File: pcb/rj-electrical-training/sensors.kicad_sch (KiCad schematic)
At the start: 13 parts, among them IC1 IS31FL3254-QFLS4-TR, IC2 LM75ADP,118, U10 TMAG5273C1QDBVR, U7 ICM-42605, U8 VEML3328, U9 TCA9534PWR

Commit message: Updated sensor schematics and GPIO expander
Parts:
- added C27: 0.1u, TMAG5273C1QDBVR:SOT95P280X140-6N, symbol Device:C
- added C28: 1u, TMAG5273C1QDBVR:SOT95P280X140-6N, symbol Device:C
- added C29: 100nF, TMAG5273C1QDBVR:SOT95P280X140-6N, symbol Device:C
- added LED1, LED2, LED4, LED5, LED6, LED7, LED8, LED9: CLMVC-FKA-CL1D1L71BB7C3C3, CLMVC-FKA-CL1D1L71BB7C3C3_CRE, symbol 2026-10-25_23-53-28:CLMVC-FKA-CL1D1L71BB7C3C3
- added RN1: YC158TJR-0710KL, YC158TJR-0710KL:RESCAXE64P320X160X70-10N, symbol YC158TJR-0710KL:YC158TJR-0710KL
- added S1: DS01C-254-L-08BE, DS01C-254-L-08BE:SW_DS01C-254-L-08BE, symbol DS01C-254-L-08BE:DS01C-254-L-08BE
- C24: value 100nF -> 100n
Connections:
- net 3.3V: now also IC1.26 (SDB), C27.1, C28.1, C29.1, LED1.1, LED2.1, LED4.1, LED5.1, LED6.1, LED7.1, LED8.1, LED9.1, RN1.10, RN1.5
- net GND: now also IC1.27 (AD), IC1.33 (EP), R24.2, C27.2, C28.2, C29.2, S1.1B, S1.2B, S1.3B, S1.4B, S1.5B, S1.6B, S1.7B, S1.8B; no longer R24.1
- net at U9.10 (P5): now also RN1.7, S1.6A
- net at U9.11 (P6): now also RN1.8, S1.7A
- net at U9.12 (P7): now also RN1.9, S1.8A
- net at U9.4 (P0): now also RN1.1, S1.1A
- net at U9.5 (P1): now also RN1.2, S1.2A
- net at U9.6 (P2): now also RN1.3, S1.3A
- net at U9.7 (P3): now also RN1.4, S1.4A
- net at U9.9 (P4): now also RN1.6, S1.5A
- net at IC1.1 (OUT1_B1): now also LED1.4
- net at IC1.10 (OUT10_R4): now also LED7.4
- net at IC1.11 (OUT11_G4): now also LED7.3
- net at IC1.12 (OUT12_B4): now also LED7.2
- net at IC1.14 (OUT13_R5): now also LED8.4
- net at IC1.15 (OUT14_G5): now also LED8.3
- net at IC1.16 (OUT15_B5): now also LED8.2
- net at IC1.17 (OUT16_R6): now also LED4.4
- net at IC1.18 (OUT17_R6): now also LED4.3
- net at IC1.19 (OUT18_G6): now also LED4.2
- net at IC1.2 (OUT2_R1): now also LED1.3
- net at IC1.20 (OUT19_B7): now also LED6.4
- net at IC1.21 (OUT20_R7): now also LED6.3
- net at IC1.22 (OUT21_R7): now also LED6.2
- net at IC1.23 (OUT22_G8): now also LED9.4
- net at IC1.24 (OUT23_B8): now also LED9.3
- net at IC1.25 (OUT24_R8): now also LED9.2
- net at IC1.3 (OUT3_G1): now also LED1.2
- net at IC1.30 (ISET): now also R24.1; no longer R24.2
- net at IC1.4 (OUT4_B2): now also LED2.4
- net at IC1.5 (OUT5_B2): now also LED2.3
- net at IC1.6 (OUT6_R2): now also LED2.2
- net at IC1.7 (OUT7_G3): now also LED5.4
- net at IC1.8 (OUT8_B3): now also LED5.3
- net at IC1.9 (OUT9_B3): now also LED5.2
- no-connect marks 1 -> 4
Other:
- note added: "GPIO Expander"
- note added: "LED Controller"
- moved on the sheet: C25, R24, U10, U9

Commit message: Integrated LEDs to circuit
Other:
- company: (none) -> RoboJackets Mini Project
- title: (none) -> Sensors
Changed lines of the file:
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@@
 	(generator_version "10.0")
 	(paper "A4")
+	(title_block
+		(title "Sensors")
+		(date "2026-10-27")
+		(rev "V2")
+		(company "RoboJackets Mini Project")
+		(comment 1 "Isa Baig")
+	)
 	(rectangle
 		(start 127 127)
@@
 	)
 	(junction
+		(at 233.68 29.21)
+		(diameter 0)
+		(color 0 0 0 0)
+	)
+	(junction
 		(at 232.41 66.04)
 		(diameter 0)
@@
 	(wire
 		(pts
+			(xy 233.68 21.59) (xy 233.68 29.21)
+		)
+		(stroke
+			(width 0)
+			(type default)
+		)
+	)
+	(wire
+		(pts
 			(xy 69.85 110.49) (xy 69.85 114.3)
 		)
@@
 	(wire
 		(pts
-			(xy 218.44 29.21) (xy 236.22 29.21)
+			(xy 218.44 29.21) (xy 233.68 29.21)
 		)
 		(stroke
@@
 	(wire
 		(pts
+			(xy 233.68 29.21) (xy 236.22 29.21)
+		)
+		(stroke
+			(width 0)
+			(type default)
+		)
+	)
+	(wire
+		(pts
 			(xy 88.9 109.22) (xy 91.44 109.22)
 		)
@@
 		)
 	)
+	(hierarchical_label "color_sensor_led"
+		(shape output)
+		(at 233.68 21.59 0)
+		(effects
+			(font
+				(size 1.27 1.27)
+			)
+			(justify left)
+		)
+	)
 	(symbol
 		(lib_id "2026-10-25_23-53-28:CLMVC-FKA-CL1D1L71BB7C3C3")
@@
 		(in_pos_files yes)
 		(dnp no)
-		(fields_autoplaced yes)
 		(property "Reference" "LED5"
 			(at 194.31 107.95 0)
@@
 		)
 		(property "Value" "CLMVC-FKA-CL1D1L71BB7C3C3"
-			(at 194.31 110.49 0)
+			(at 181.61 108.966 0)
 			(show_name no)
 			(do_not_autoplace no)
@@
 		(dnp no)
 		(property "Reference" "LED2"
-			(at 194.31 100.33 0)
+			(at 178.054 104.14 0)
 			(show_name no)
 			(do_not_autoplace no)
@@
 		)
 		(property "Value" "CLMVC-FKA-CL1D1L71BB7C3C3"
-			(at 184.658 123.698 0)
+			(at 179.578 123.444 0)
 			(show_name no)
 			(do_not_autoplace no)

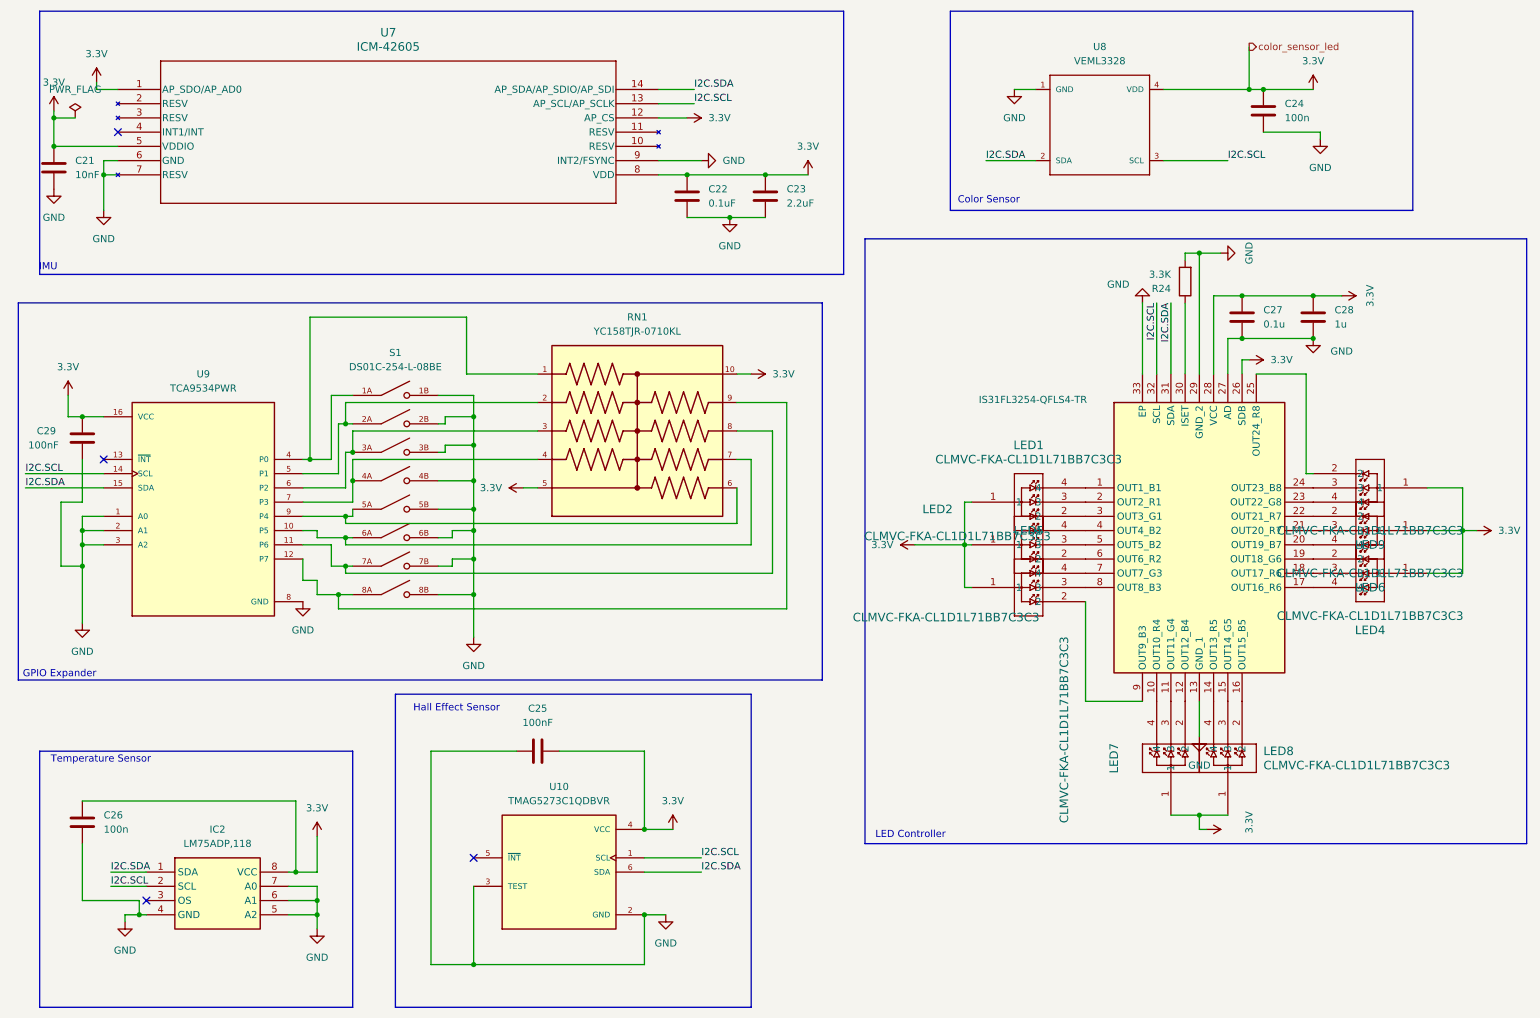
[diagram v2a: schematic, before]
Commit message: Separate SDA SCL
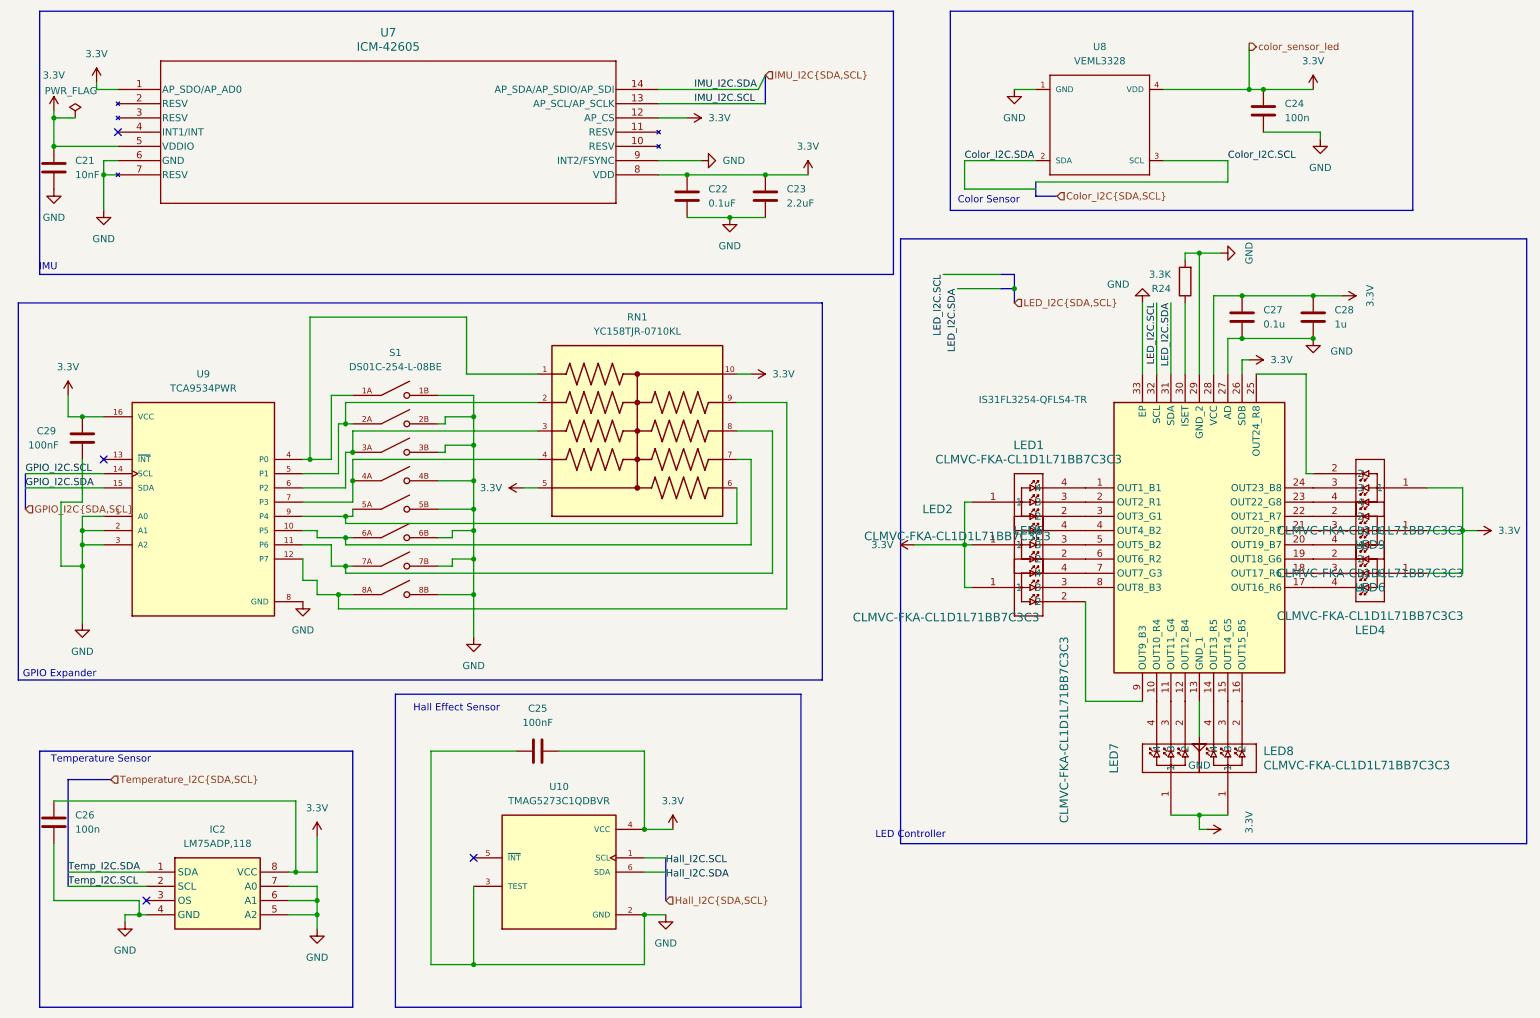
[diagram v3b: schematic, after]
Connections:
- removed net I2C.SCL: IC1.32 (SCL), IC2.2 (SCL), U10.1 (SCL), U7.13 (AP_SCL/AP_SCLK), U8.3 (SCL), U9.14 (SCL)
- removed net I2C.SDA: IC1.31 (SDA), IC2.1 (SDA), U10.6 (SDA), U7.14 (AP_SDA/AP_SDIO/AP_SDI), U8.2 (SDA), U9.15 (SDA)
- new net Color_I2C.SCL: U8.3 (SCL)
- new net Color_I2C.SDA: U8.2 (SDA)
- new net GPIO_I2C.SCL: U9.14 (SCL)
- new net GPIO_I2C.SDA: U9.15 (SDA)
- new net IMU_I2C.SCL: U7.13 (AP_SCL/AP_SCLK)
- new net IMU_I2C{SDA,SCL}: U7.14 (AP_SDA/AP_SDIO/AP_SDI)
- new net LED_I2C.SCL: IC1.32 (SCL)
- new net LED_I2C.SDA: IC1.31 (SDA)
- new net Temp_I2C.SCL: IC2.2 (SCL)
- new net Temp_I2C.SDA: IC2.1 (SDA)
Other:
- moved on the sheet: C26
